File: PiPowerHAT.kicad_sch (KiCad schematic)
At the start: 34 parts, among them J1 2444, J3 Conn_01x02, J6 Raspberry_Pi_2_3, J8 2444, Q1 AO3401A, Q2 MMDT5401, Q3 DMG2305UX-13, U1 XL4015

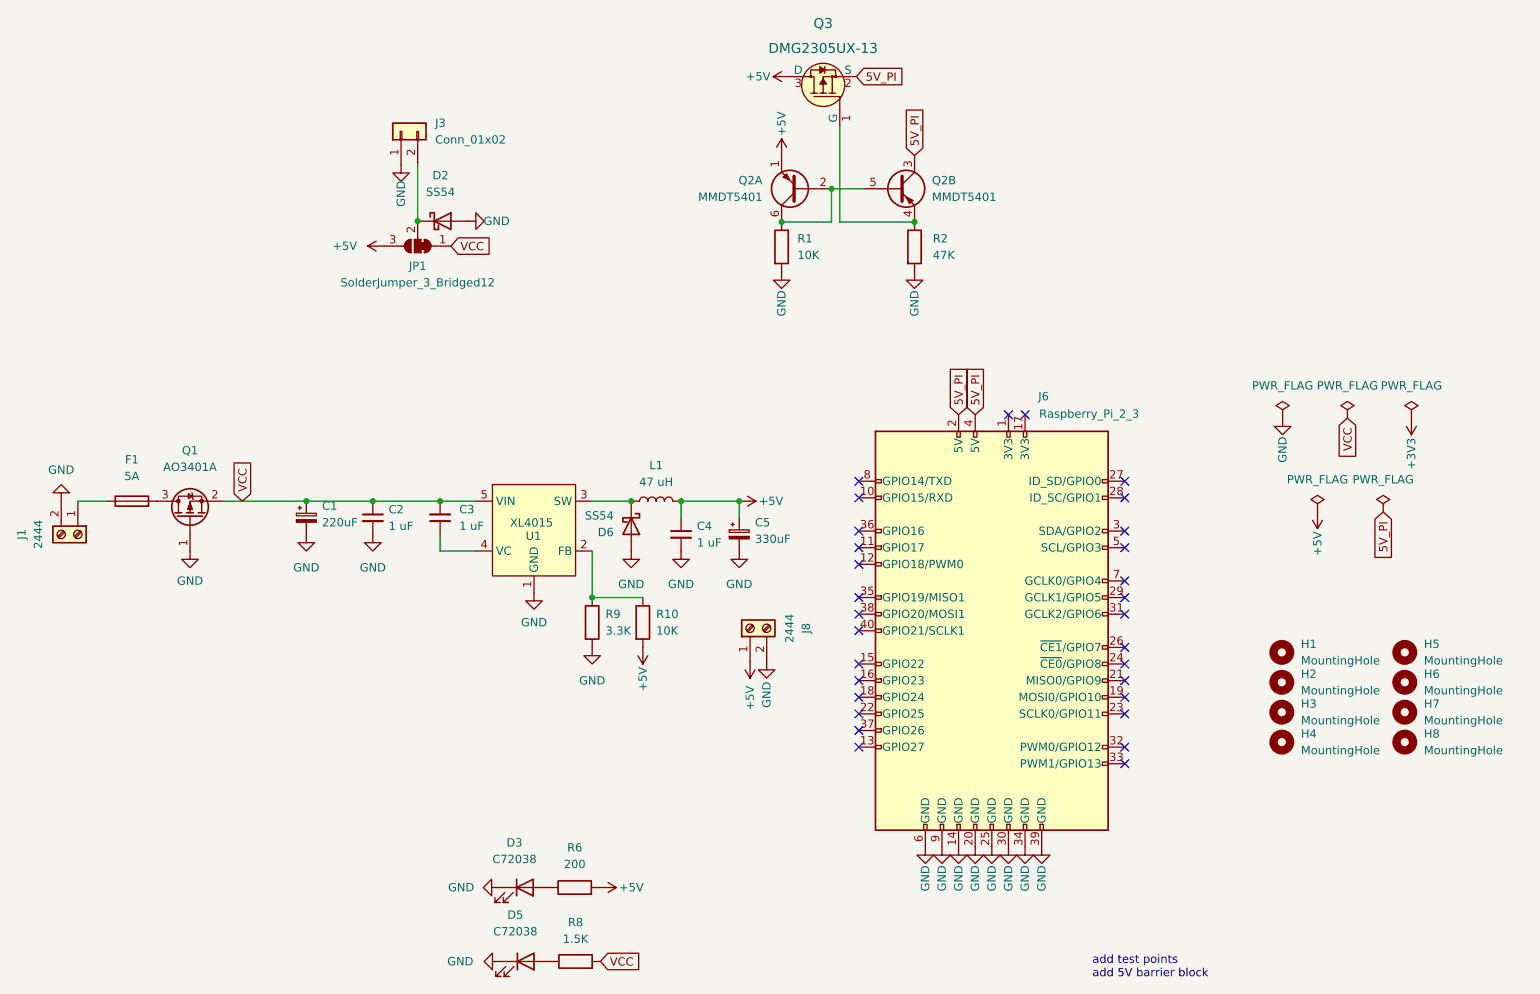
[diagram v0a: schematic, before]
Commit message: Cleanup and miscellaneous changes. Changed fuseholder and FET
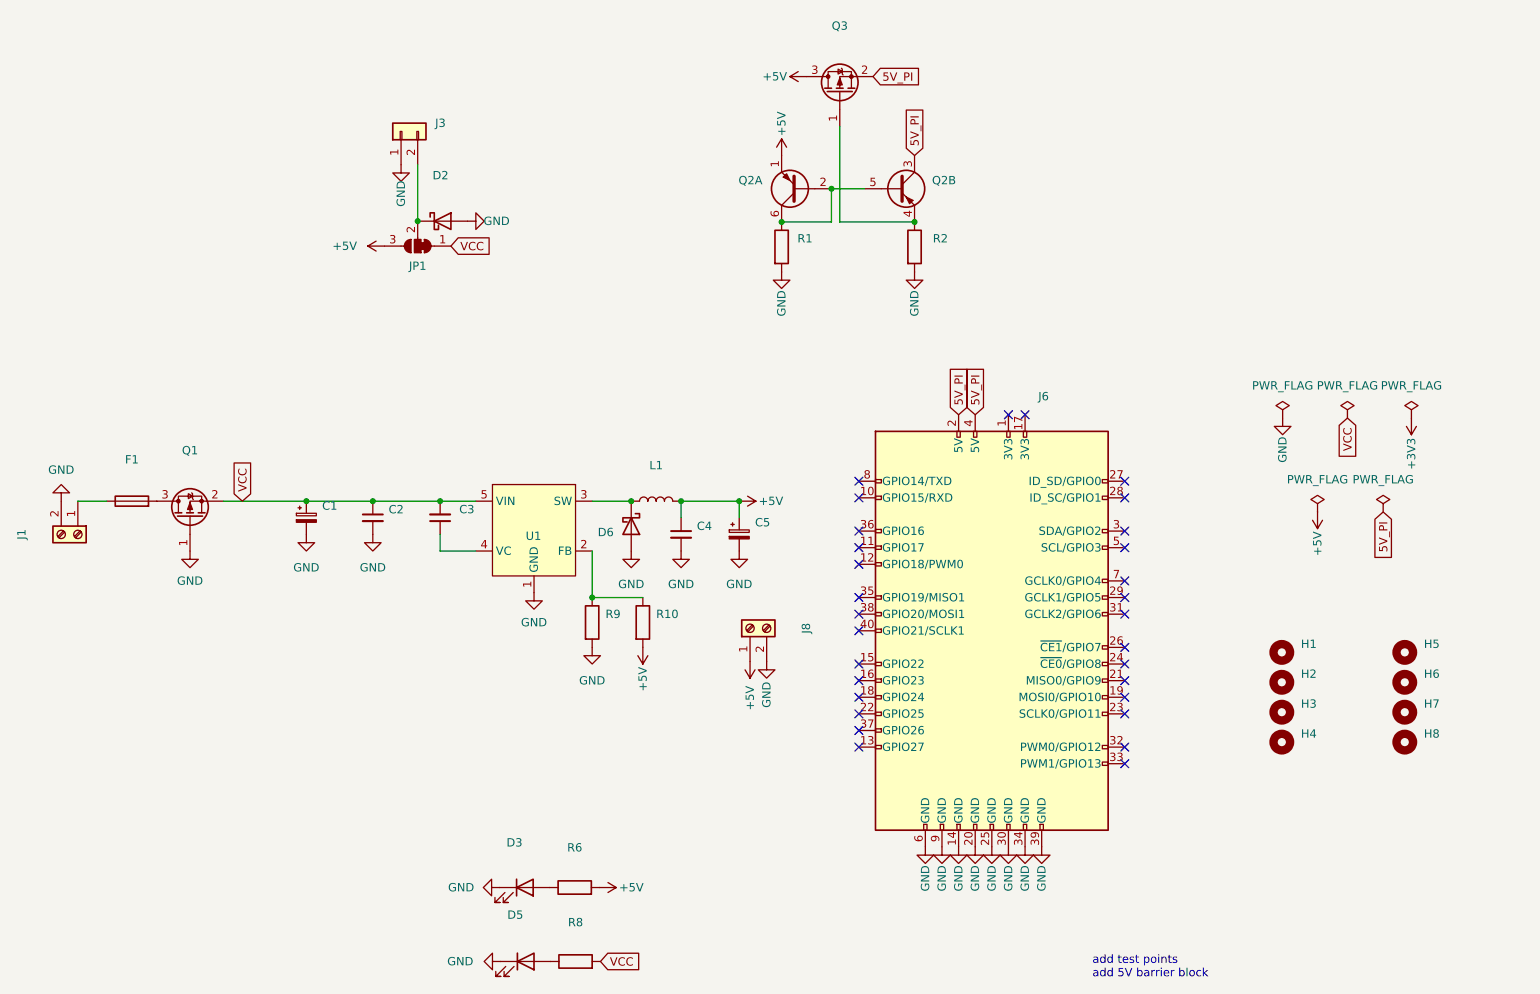
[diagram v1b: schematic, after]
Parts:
- removed Q3: DMG2305UX-13, digikey-footprints:SOT-23-3, symbol dk_Transistors-FETs-MOSFETs-Single:DMG2305UX-13
- added Q3: (no value), symbol Transistor_FET:AO3401A
- C1: value 220uF -> (none); footprint Capacitor_SMD:CP_Elec_10x10 -> (none)
- C2, C3, C4: value 1 uF -> (none); footprint Capacitor_SMD:C_0603_1608Metric -> (none)
- C5: value 330uF -> (none); footprint Capacitor_SMD:CP_Elec_6.3x7.7 -> (none)
- D2, D6: value SS54 -> (none); footprint Diode_SMD:D_SMA -> (none); JLC (none) -> C22452
- D3, D5: value C72038 -> (none); footprint LED_SMD:LED_0603_1608Metric -> (none); JLC (none) -> C72038
- F1: value 5A -> (none); footprint Fuse:Fuseholder_Littelfuse_Nano2_154x -> (none)
- H1, H2, H3, H4: value MountingHole -> (none); footprint MountingHole:MountingHole_2.7mm_M2.5_DIN965_Pad -> (none)
- H5, H6, H7, H8: value MountingHole -> (none); footprint MountingHole:MountingHole_3.5mm -> (none)
- J1, J8: value 2444 -> (none); footprint TerminalBlock_4Ucon:TerminalBlock_4Ucon_1x02_P3.50mm_Horizontal -> (none)
- J3: value Conn_01x02 -> (none); footprint Connector_JST:JST_XH_B2B-XH-A_1x02_P2.50mm_Vertical -> (none)
- J6: value Raspberry_Pi_2_3 -> (none); footprint Connector_PinHeader_2.54mm:PinHeader_2x20_P2.54mm_Vertical -> (none)
- JP1: value SolderJumper_3_Bridged12 -> (none); footprint Jumper:SolderJumper-3_P1.3mm_Bridged2Bar12_RoundedPad1.0x1.5mm -> (none)
- L1: value 47 uH -> (none); footprint Inductor_SMD:L_12x12mm_H6mm -> (none); JLC YSPI1365-470M -> C497913
- Q1: value AO3401A -> (none); footprint Package_TO_SOT_SMD:SOT-23 -> (none); JLC (none) -> C15127
- Q2: value MMDT5401 -> (none); footprint Package_TO_SOT_SMD:SOT-363_SC-70-6 -> (none); JLC (none) -> C54540
- R1: value 10K -> (none); footprint Resistor_SMD:R_0402_1005Metric -> (none); JLC (none) -> C25804
- R10: value 10K -> (none); footprint Resistor_SMD:R_0603_1608Metric -> (none)
- R2: value 47K -> (none); footprint Resistor_SMD:R_0402_1005Metric -> (none)
- R6: value 200 -> (none); footprint Resistor_SMD:R_0402_1005Metric -> (none)
- R8: value 1.5K -> (none); footprint Resistor_SMD:R_0402_1005Metric -> (none)
- R9: value 3.3K -> (none); footprint Resistor_SMD:R_0603_1608Metric -> (none)
- U1: value XL4015 -> (none); footprint Package_TO_SOT_SMD:TO-263-5_TabPin3 -> (none); JLC (none) -> C51661
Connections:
- net +5V: now also Q3.3 (D)
- net 5V_PI: now also Q3.2 (S)
- net at Q2.4 (E2), R2.1: now also Q3.1 (G)

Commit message: Minor Updates and Cleaning
Changed JLC field to LCSC
Changed Aux power output to JST XH
Small changes to silkscreen labels to hide below components once fitted
Added connector name labels to Frontsilk
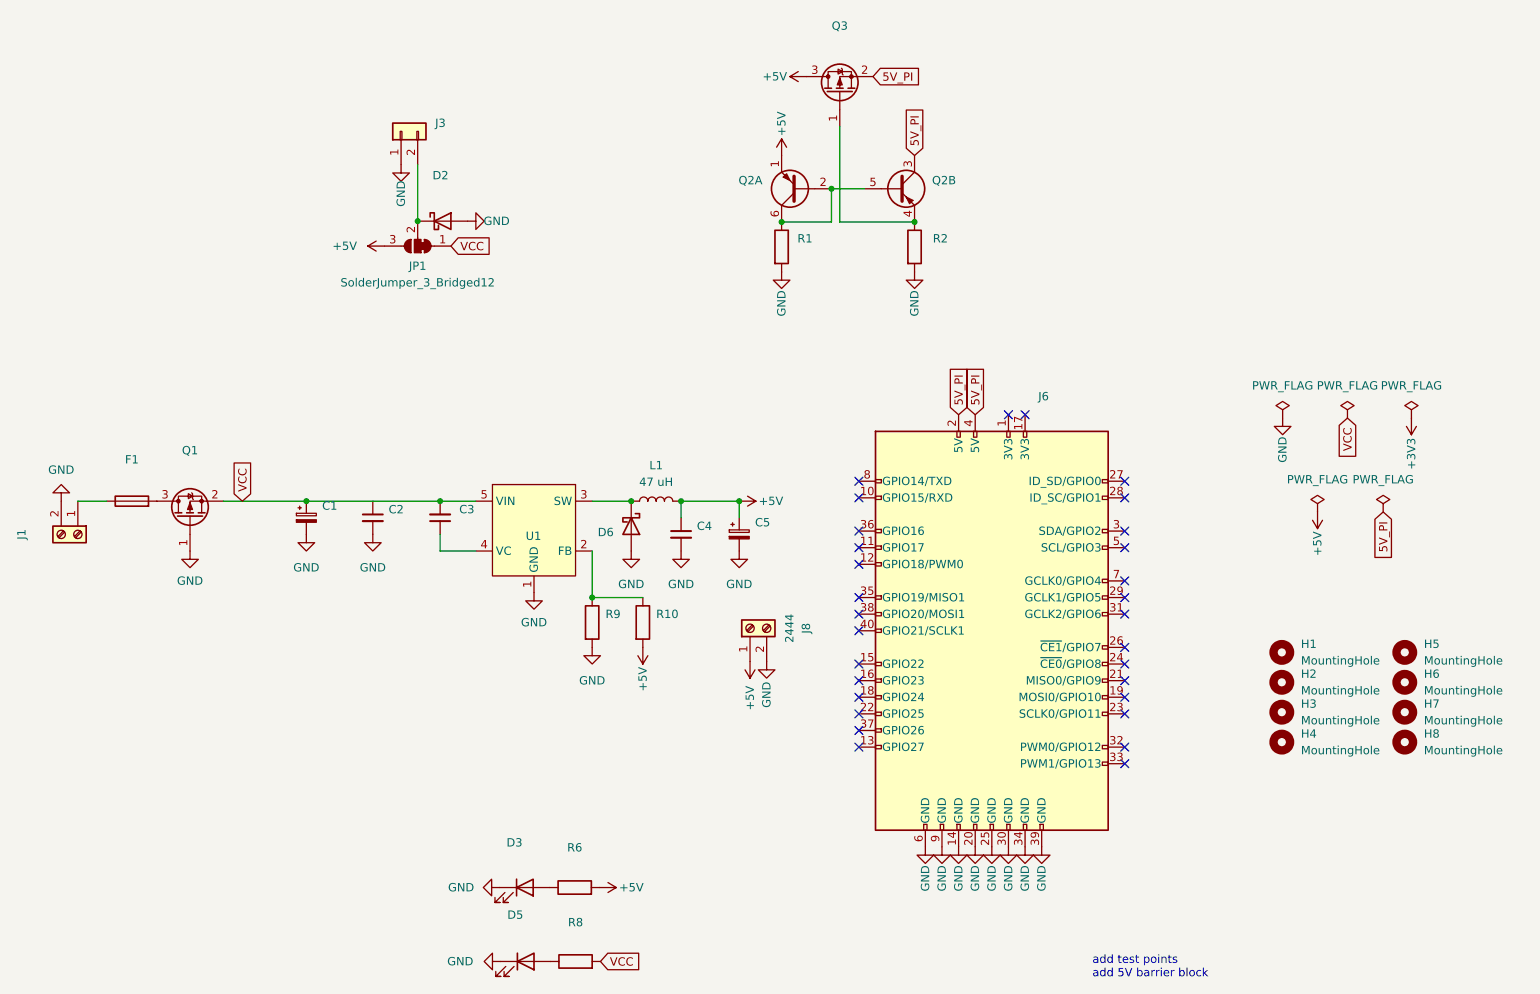
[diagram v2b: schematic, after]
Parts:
- C1: JLC C176670 -> (none); LCSC (none) -> C176670
- C2, C3, C4: JLC C15849 -> (none); LCSC (none) -> C15849
- C5: JLC C58277 -> (none); LCSC (none) -> C58277
- D2, D6: JLC C22452 -> (none); LCSC (none) -> C22452
- D3, D5: JLC C72038 -> (none); LCSC (none) -> C72038
- F1: JLC C206916 -> (none); LCSC (none) -> C206916
- H1, H2, H3, H4: value (none) -> MountingHole; footprint (none) -> MountingHole:MountingHole_2.7mm_M2.5_DIN965_Pad
- H5, H6, H7, H8: value (none) -> MountingHole; footprint (none) -> MountingHole:MountingHole_3.5mm
- J8: value (none) -> 2444; footprint (none) -> TerminalBlock_4Ucon:TerminalBlock_4Ucon_1x02_P3.50mm_Horizontal
- JP1: value (none) -> SolderJumper_3_Bridged12; footprint (none) -> Jumper:SolderJumper-3_P1.3mm_Bridged2Bar12_RoundedPad1.0x1.5mm
- L1: value (none) -> 47 uH; footprint (none) -> Inductor_SMD:L_12x12mm_H6mm
- Q1, Q3: JLC C15127 -> (none); LCSC (none) -> C15127
- Q2: JLC C54540 -> (none); LCSC (none) -> C54540
- R1, R10: JLC C25804 -> (none); LCSC (none) -> C25804
- R2: JLC C25792 -> (none); LCSC (none) -> C25792
- R6: JLC C25087 -> (none); LCSC (none) -> C25087
- R8: JLC C25867 -> (none); LCSC (none) -> C25867
- R9: JLC C22978 -> (none); LCSC (none) -> C22978
- U1: JLC C51661 -> (none); LCSC (none) -> C51661
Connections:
- net VCC: no longer C2.1
